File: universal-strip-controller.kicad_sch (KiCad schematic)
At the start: 54 parts, among them J1 Conn_01x03_Pin, J2 Conn_01x02_Pin, SW1 434133025816, SW2 434133025816, U1 RP2350B, U2 RPI RM2, U3 W25Q128JVSIQ, U9 DS3231SN, X1 12MHz

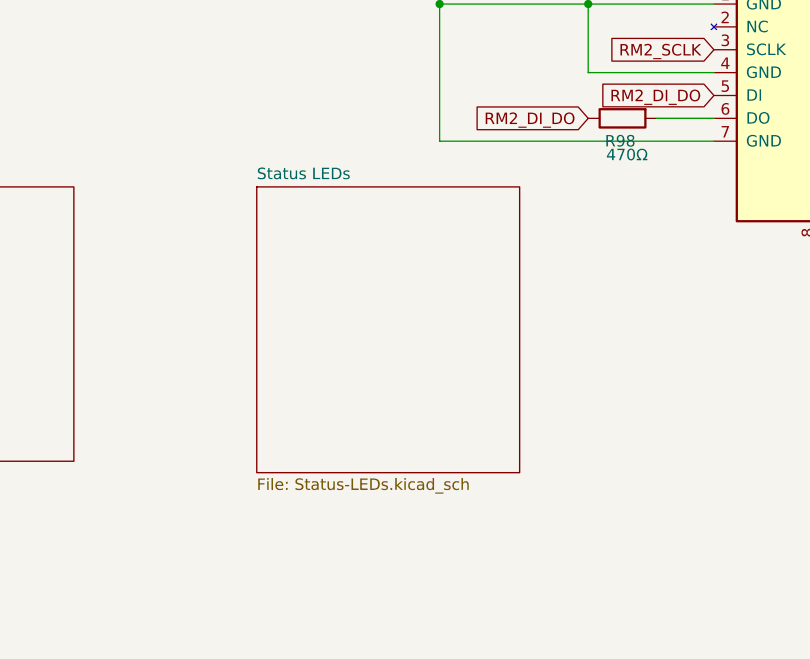
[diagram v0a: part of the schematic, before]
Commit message: Did away with the status LEDs for now, too much real estate
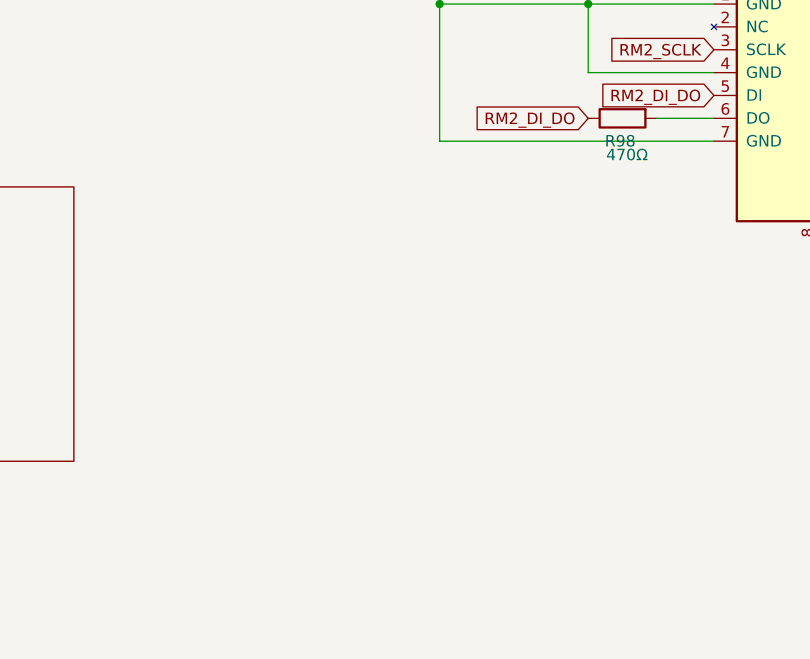
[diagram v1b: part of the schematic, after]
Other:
- removed sheet Status LEDs
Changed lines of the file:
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@@
-	)
-	(sheet
-		(at 284.48 208.28)
-		(size 29.21 31.75)
-		(exclude_from_sim no)
-		(in_bom yes)
-		(on_board yes)
-		(dnp no)
-		(fields_autoplaced yes)
-		(stroke
-			(width 0.1524)
-			(type solid)
-		)
-		(fill
-			(color 0 0 0 0)
-		)
-		(property "Sheetname" "Status LEDs"
-			(at 284.48 207.5684 0)
-			(show_name no)
-			(do_not_autoplace no)
-			(effects
-				(font
-					(size 1.27 1.27)
-				)
-				(justify left bottom)
-			)
-		)
-		(property "Sheetfile" "Status-LEDs.kicad_sch"
-			(at 284.48 240.6146 0)
-			(show_name no)
-			(do_not_autoplace no)
-			(effects
-				(font
-					(size 1.27 1.27)
-				)
-				(justify left top)
-			)
-		)
-		(instances
-			(project "universal-strip-controller"
-				(path "/b1a25501-925f-4082-acf3-9513bc59c329"
-					(page "3")
-				)
-			)
-		)
 	)
 	(sheet
